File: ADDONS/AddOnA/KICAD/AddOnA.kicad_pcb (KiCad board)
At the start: 2 copper layers, 178 x 39 mm, 55 parts, among them IC1 FIN1002, IC101 74HC251, IC6 PCA9536D, P1 10K0, SW1 Switch_DPDT, SW2 Switch_DPDT, X1 RCA, X101 XLR3, X110 PLR135_T10, X114 CON_IDC26, X115 CON_IDC26, X2 XLR3, X3 RCA, X4 Conn_01x03, X5 MicroMatch14, X6 HDR_02x08, X7 PLT133_T10W, X8 CON_USB_B, X9 USB_A

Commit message: Updated Gerbers
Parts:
- added REF**: WEEE-Logo_5.6x8mm_SilkScreen, Symbol:WEEE-Logo_5.6x8mm_SilkScreen, B.Cu at (179.0, -69.0)
- added REF**: CE-Logo_8.5x6mm_SilkScreen, Symbol:CE-Logo_8.5x6mm_SilkScreen, B.Cu at (170.0, -70.0)
- X9: value USB_A -> HDR_01x05; footprint Connector_USB:USB_A_CNCTech_1001-011-01101_Horizontal -> Connector_PinHeader_2.54mm:PinHeader_1x05_P2.54mm_Vertical
- moved X9 7.02 mm to (26.1, -52.9)
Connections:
- IC101 pad 10: /DIGSEL:1 -> +3V3
- IC101 pad 11: /DIG_RIGHT -> +3V3
- IC101 pad 12: GND -> Net-(IC101-Pad12)
- IC101 pad 13: Net-(IC101-Pad13) -> Net-(C17-Pad2)
- IC101 pad 14: Net-(C17-Pad2) -> GND
- IC101 pad 7: /DIG_LEFT -> GND
- R6 pad 2: Net-(IC101-Pad13) -> Net-(IC101-Pad12)
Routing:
- net /DIG_LEFT: track 53.2 -> 22.4 mm
- net /DIGSEL:1: track 67.9 -> 43.1 mm
- net /DIG_RIGHT: track 36.7 -> 14.5 mm
- net +3V3: track 154.5 -> 166.6 mm
- net Net-(IC101-Pad12): track 0.00 -> 11.2 mm
- net Net-(IC101-Pad13): track 9.96 -> 0.00 mm
- net Net-(X8-Pad1): track 30.5 -> 36.5 mm
- net Net-(X8-Pad4): track 24.1 -> 28.0 mm
- net /D+: track 24.6 -> 28.5 mm
- net /D-: track 24.1 -> 28.0 mm
- net GND: track 26.6 -> 28.8 mm, vias 24 -> 25
- net Net-(C17-Pad2): track 7.68 -> 6.86 mm
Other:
- board text added: "AddOn A auverdion 1.0.0"

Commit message: Minor changes on AddOn A
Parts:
- removed REF**: WEEE-Logo_5.6x8mm_SilkScreen, Symbol:WEEE-Logo_5.6x8mm_SilkScreen
- removed REF**: CE-Logo_8.5x6mm_SilkScreen, Symbol:CE-Logo_8.5x6mm_SilkScreen
- moved R11 2.00 mm to (80.7, -78.7)
- moved R12 2.00 mm to (71.3, -78.7)
- moved R13 2.00 mm to (94.7, -78.7)
- moved R14 2.00 mm to (85.3, -78.7)
- moved SW1 2.00 mm to (76.0, -88.0)
- moved SW2 2.00 mm to (90.0, -88.0)
- moved B1 1.50 mm to (180.0, -91.5)
- moved B2 1.50 mm to (10.0, -91.5)
- moved C1 1.50 mm to (62.4, -81.6)
- moved C101 1.50 mm to (157.7, -79.7)
- moved C109 1.50 mm to (53.9, -83.5)
- moved C113 1.50 mm to (51.5, -79.2)
- moved C17 1.50 mm to (43.8, -80.9)
- moved C2 1.50 mm to (65.9, -77.6)
- moved C3 1.50 mm to (62.4, -75.6)
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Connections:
- IC101 pad 1: GND -> Net-(C17-Pad2)
- IC101 pad 13: Net-(C17-Pad2) -> GND
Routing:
- net Net-(C17-Pad2): track 6.86 -> 17.1 mm
- net +3V3: track 166.6 -> 161.8 mm
- net /DIG_RIGHT: track 14.5 -> 16.7 mm
- net /DIGSEL:1: track 43.1 -> 44.9 mm
- net GND: track 28.8 -> 30.5 mm
- net /D+: track 28.5 -> 30.0 mm
- net Net-(X8-Pad4): track 28.0 -> 29.5 mm
- net Net-(X8-Pad1): track 36.5 -> 38.0 mm
- net /SPDIF_TX: track 80.6 -> 82.1 mm
- net /SPDIF_RX: track 63.8 -> 65.3 mm
- net /AOUT1+: track 18.8 -> 20.3 mm
- net /AIN5+: track 43.3 -> 44.8 mm
- net /AIN1-: track 45.6 -> 47.1 mm
- net /AIN1+: track 40.7 -> 42.2 mm
- net /AOUT1-: track 15.5 -> 17.0 mm
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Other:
- board text added: "AddOn A auverdion 1.0.1"
- board text removed: "AddOn A auverdion 1.0.0"

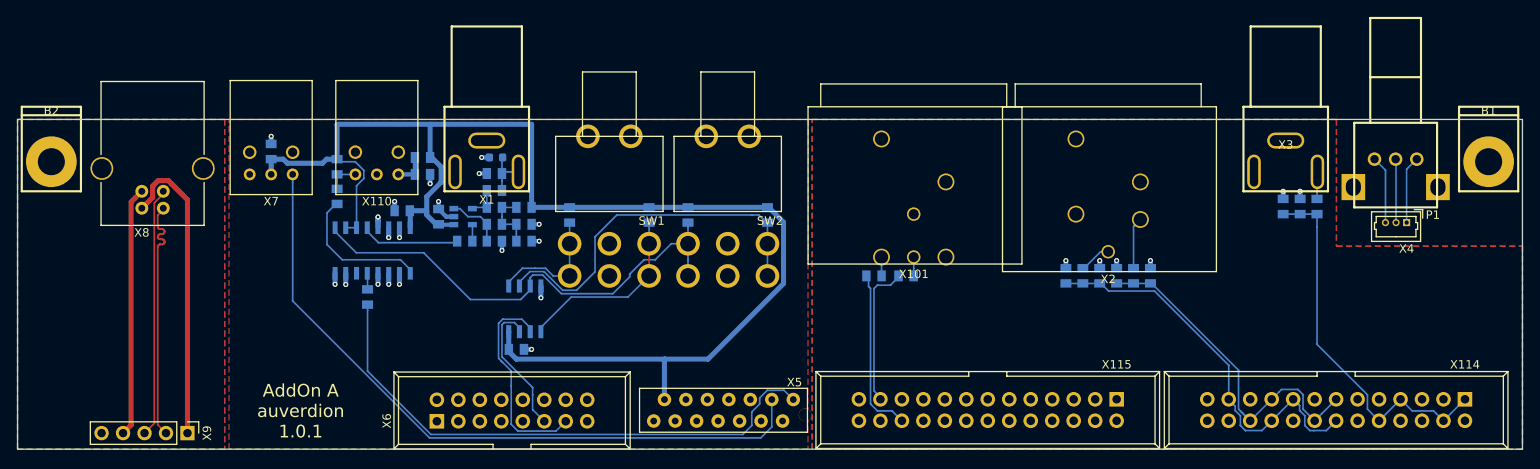
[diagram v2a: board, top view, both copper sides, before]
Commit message: Mechanical redefinition of board edges AddOnA
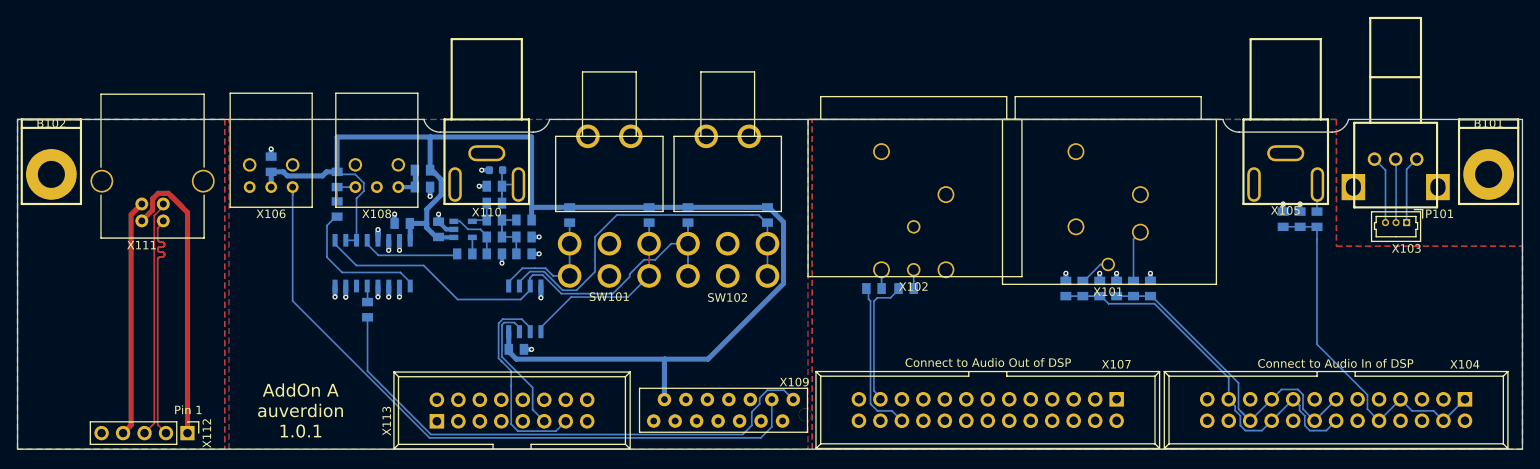
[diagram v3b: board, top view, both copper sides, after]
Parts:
- removed P1: 10K0, rklib:RK09K1110-20
- added P101: 10K0, rklib:RK09K1110-20, F.Cu at (169.0, -82.0)
- added REF**: WEEE-Logo_4.2x6mm_SilkScreen, Symbol:WEEE-Logo_4.2x6mm_SilkScreen, B.Cu at (169.0, -68.0)
- added REF**: CE-Logo_8.5x6mm_SilkScreen, Symbol:CE-Logo_8.5x6mm_SilkScreen, B.Cu at (177.0, -68.0)
- moved B101 1.50 mm to (180.0, -90.0)
- moved B102 1.50 mm to (10.0, -90.0)
- moved C101 1.50 mm to (140.0, -70.0)
- moved C102 1.50 mm to (134.0, -70.0)
- moved C104 1.50 mm to (157.7, -78.2)
- moved C105 1.50 mm to (36.0, -84.7)
- moved C106 1.50 mm to (53.9, -82.0)
- moved C107 1.50 mm to (43.8, -79.4)
- moved C108 1.50 mm to (62.4, -80.1)
- moved C109 1.50 mm to (65.9, -76.1)
- moved C110 1.50 mm to (62.4, -74.1)
- moved C111 1.50 mm to (55.8, -77.0)
- moved C112 1.50 mm to (51.5, -77.7)
- moved D101 1.50 mm to (62.6, -84.0)
- moved IC102 1.50 mm to (48.0, -73.0)
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- renumbered B1 to B101, B2 to B102, C5 to C101, C6 to C102, C24 to C103, C101 to C104, C7 to C105, C109 to C106, C17 to C107, C1 to C108, C2 to C109, C3 to C110, C4 to C111, C113 to C112, D1 to D101, IC6 to IC101, IC101 to IC102, IC1 to IC103, R7 to R101, R8 to R102, R101 to R103, R9 to R104, R102 to R105, R10 to R106, R117 to R107, R118 to R108, R11 to R109, R12 to R110, R25 to R111, R29 to R112, R4 to R113, R1 to R114, R6 to R115, R2 to R116, R5 to R117, R3 to R118, R13 to R119, R14 to R120, SW1 to SW101, SW2 to SW102, X2 to X101, X101 to X102, X4 to X103, X114 to X104, X3 to X105, X7 to X106, X115 to X107, X110 to X108, X5 to X109, X1 to X110, X8 to X111, X9 to X112, X6 to X113
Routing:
- net /D-: track 29.5 -> 28.0 mm
- net Net-(X111-Pad1): track 38.0 -> 36.5 mm
- net /SPDIF_RX: track 65.3 -> 63.8 mm
- net /D+: track 30.0 -> 28.5 mm
- net /AOUT1+: track 20.3 -> 18.8 mm
- net /AIN1-: track 47.1 -> 45.6 mm
- net /AIN1+: track 42.2 -> 40.7 mm
- net /AOUT1-: track 17.0 -> 15.5 mm
- net Net-(X111-Pad4): track 29.5 -> 28.0 mm
- net /AIN5+: track 44.8 -> 43.3 mm
- net /DIGSEL:0: track 57.4 -> 56.8 mm
- added copper zone on B.Cu, net (none)
- removed copper zone on B.Cu, net Net-(X111-Pad5)
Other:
- outline, holes or cut-outs redrawn
- board text added: "Connect to Audio In of DSP"
- board text added: "Connect to Audio Out of DSP"
- board text added: "Pin 1"
